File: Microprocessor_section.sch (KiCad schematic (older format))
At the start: 14 parts

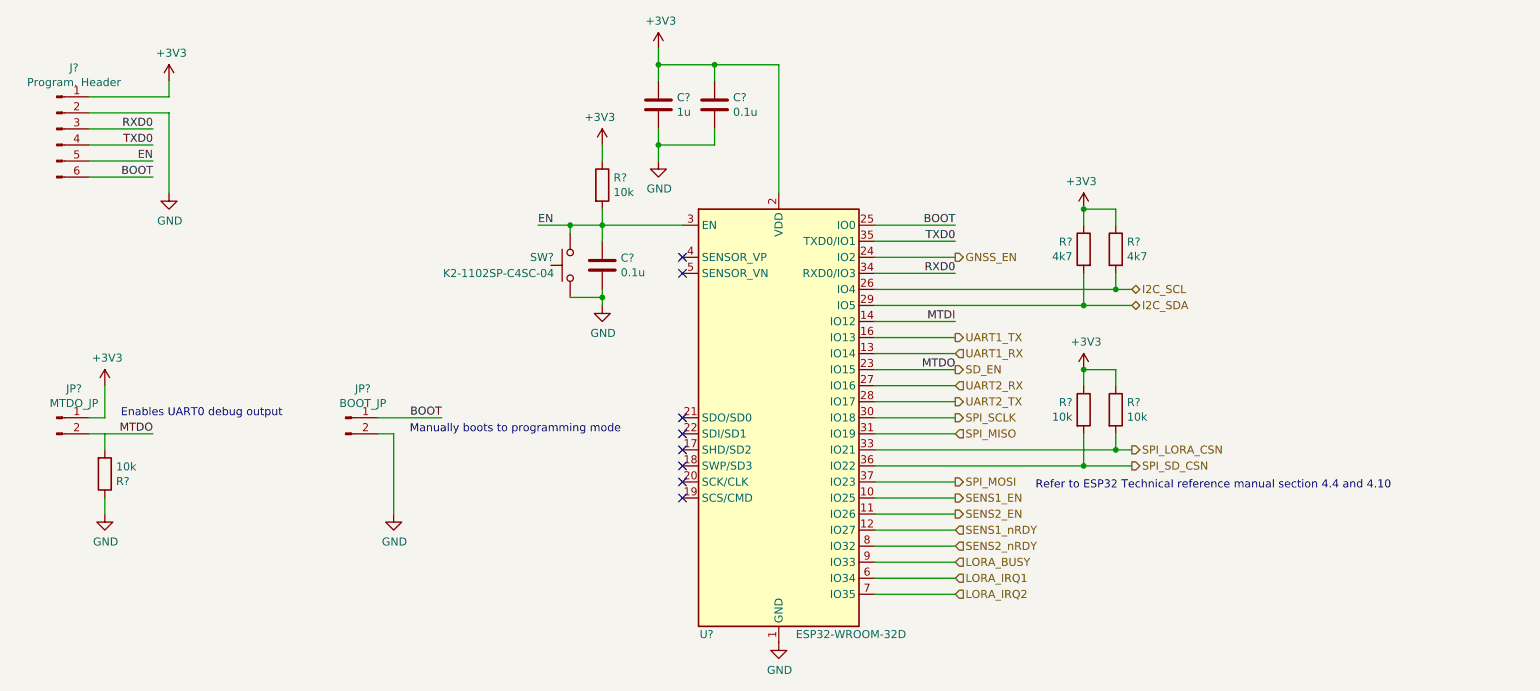
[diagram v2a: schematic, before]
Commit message: Change BME280 out for connector
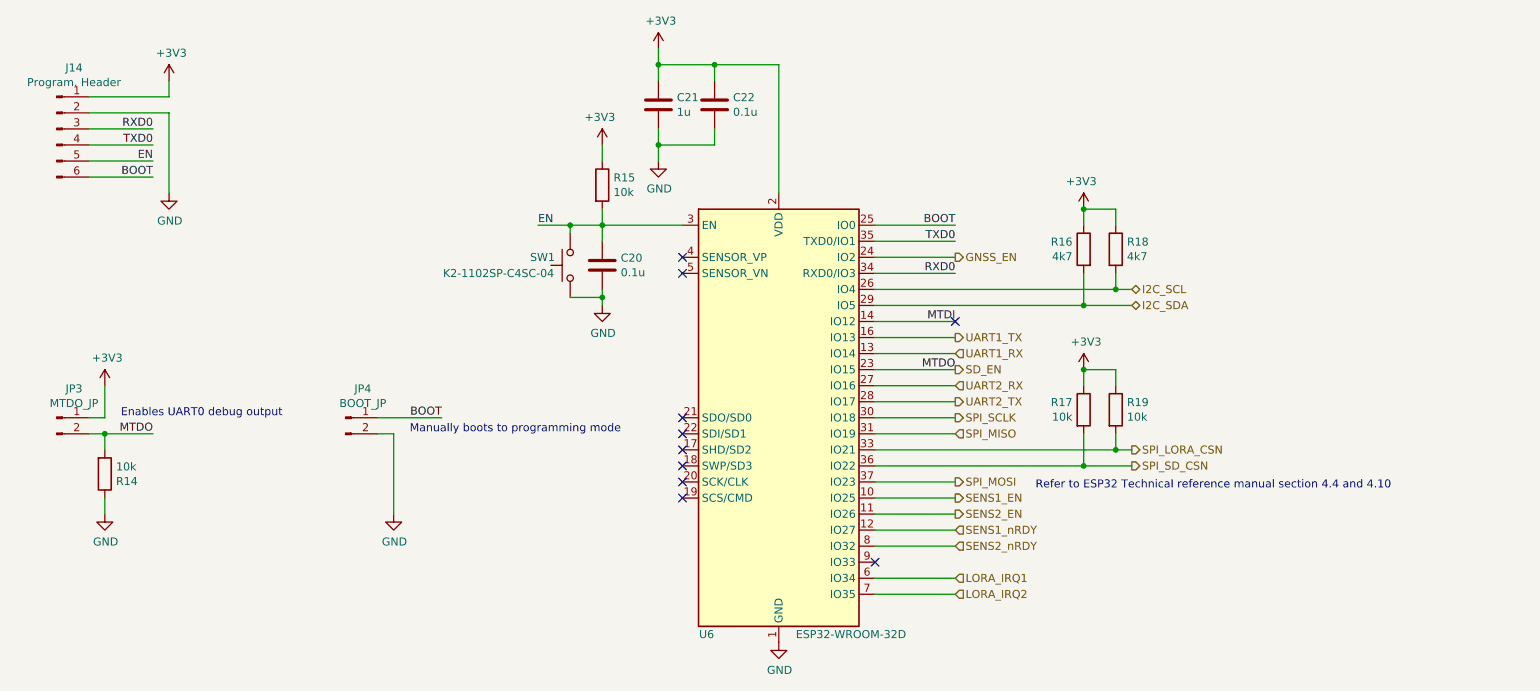
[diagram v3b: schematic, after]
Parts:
- gave numbers to parts that had none: 14
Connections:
- net SD_EN: now also R14.2
- net LORA_BUSY: no longer names the net of U6.9 (IO33)
- no-connect marks 8 -> 10
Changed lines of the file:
@@
 $EndDescr
 $Comp
-L power:GND #PWR?
+L power:GND #PWR060
 U 1 1 60B1C531
 P 2700 2600
-F 0 "#PWR?" H 2700 2350 50  0001 C CNN
+F 0 "#PWR060" H 2700 2350 50  0001 C CNN
 F 1 "GND" H 2705 2427 50  0000 C CNN
 F 2 "" H 2700 2600 50  0001 C CNN
@@
 TXD0
 $Comp
-L Connector:Conn_01x06_Male J?
+L Connector:Conn_01x06_Male J14
 U 1 1 60B18C71
 P 2000 2200
-F 0 "J?" H 2108 2581 50  0000 C CNN
+F 0 "J14" H 2108 2581 50  0000 C CNN
 F 1 "Program. Header" H 2108 2490 50  0000 C CNN
 F 2 "" H 2000 2200 50  0001 C CNN
@@
 	2700 2000 2700 1900
 $Comp
-L power:+3V3 #PWR?
+L power:+3V3 #PWR059
 U 1 1 60A521B8
 P 2700 1900
-F 0 "#PWR?" H 2700 1750 50  0001 C CNN
+F 0 "#PWR059" H 2700 1750 50  0001 C CNN
 F 1 "+3V3" H 2715 2073 50  0000 C CNN
 F 2 "" H 2700 1900 50  0001 C CNN
@@
 	5400 3200 5400 3250
 $Comp
-L power:GND #PWR?
+L power:GND #PWR063
 U 1 1 60A62E95
 P 5400 3300
-F 0 "#PWR?" H 5400 3050 50  0001 C CNN
+F 0 "#PWR063" H 5400 3050 50  0001 C CNN
 F 1 "GND" H 5405 3127 50  0000 C CNN
 F 2 "" H 5400 3300 50  0001 C CNN
@@
 $EndComp
 $Comp
-L Device:C C?
+L Device:C C20
 U 1 1 60A615B3
 P 5400 3050
-F 0 "C?" H 5515 3096 50  0000 L CNN
+F 0 "C20" H 5515 3096 50  0000 L CNN
 F 1 "0.1u" H 5515 3005 50  0000 L CNN
 F 2 "" H 5438 2900 50  0001 C CNN
@@
 	5400 2800 5400 2700
 $Comp
-L Device:R R?
+L Device:R R15
 U 1 1 60A591EA
 P 5400 2550
-F 0 "R?" H 5470 2596 50  0000 L CNN
+F 0 "R15" H 5470 2596 50  0000 L CNN
 F 1 "10k" H 5470 2505 50  0000 L CNN
 F 2 "" V 5330 2550 50  0001 C CNN
@@
 	7100 2900 7600 2900
 $Comp
-L RF_Module:ESP32-WROOM-32D U?
+L RF_Module:ESP32-WROOM-32D U6
 U 1 1 60AF9B80
 P 6500 4000
-F 0 "U?" H 6050 2650 50  0000 C CNN
+F 0 "U6" H 6050 2650 50  0000 C CNN
 F 1 "ESP32-WROOM-32D" H 6950 2650 50  0000 C CNN
 F 2 "RF_Module:ESP32-WROOM-32" H 6500 2500 50  0001 C CNN
@@
 	8600 3700 8600 3800
 $Comp
-L power:GND #PWR?
+L power:GND #PWR066
 U 1 1 60AD4CF4
 P 6500 5400
-F 0 "#PWR?" H 6500 5150 50  0001 C CNN
+F 0 "#PWR066" H 6500 5150 50  0001 C CNN
 F 1 "GND" H 6505 5227 50  0000 C CNN
 F 2 "" H 6500 5400 50  0001 C CNN
@@
 Wire Wire Line
 	7100 5000 7600 5000
-Wire Wire Line
-	7100 4900 7600 4900
 Wire Wire Line
 	7100 4100 7600 4100
@@
 Text HLabel 7600 5000 2    50   Input ~ 0
 LORA_IRQ1
-Text HLabel 7600 4900 2    50   Input ~ 0
-LORA_BUSY
 Text HLabel 7600 3000 2    50   Output ~ 0
 GNSS_EN
@@
 	5750 2300 5750 2400
 $Comp
-L power:GND #PWR?
+L power:GND #PWR065
 U 1 1 60A601F1
 P 5750 2400
-F 0 "#PWR?" H 5750 2150 50  0001 C CNN
+F 0 "#PWR065" H 5750 2150 50  0001 C CNN
 F 1 "GND" H 5755 2227 50  0000 C CNN
 F 2 "" H 5750 2400 50  0001 C CNN
@@
 	8400 3800 8400 3700
 $Comp
-L power:+3V3 #PWR?
+L power:+3V3 #PWR068
 U 1 1 60A5A46E
 P 8400 3700
-F 0 "#PWR?" H 8400 3550 50  0001 C CNN
+F 0 "#PWR068" H 8400 3550 50  0001 C CNN
 F 1 "+3V3" H 8415 3873 50  0000 C CNN
 F 2 "" H 8400 3700 50  0001 C CNN
@@
 $EndComp
 $Comp
-L Device:R R?
+L Device:R R19
 U 1 1 60A5A468
 P 8600 3950
-F 0 "R?" H 8670 3996 50  0000 L CNN
+F 0 "R19" H 8670 3996 50  0000 L CNN
 F 1 "10k" H 8670 3905 50  0000 L CNN
 F 2 "" V 8530 3950 50  0001 C CNN
@@
 $EndComp
 $Comp
-L Device:R R?
+L Device:R R17
 U 1 1 60A5A462
 P 8400 3950
-F 0 "R?" H 8330 3996 50  0000 R CNN
+F 0 "R17" H 8330 3996 50  0000 R CNN
 F 1 "10k" H 8330 3905 50  0000 R CNN
 F 2 "" V 8330 3950 50  0001 C CNN
@@
 	8600 3200 8600 3100
 $Comp
-L power:+3V3 #PWR?
+L power:+3V3 #PWR067
 U 1 1 60A5400B
 P 8400 2700
-F 0 "#PWR?" H 8400 2550 50  0001 C CNN
+F 0 "#PWR067" H 8400 2550 50  0001 C CNN
 F 1 "+3V3" H 8415 2873 50  0000 C CNN
 F 2 "" H 8400 2700 50  0001 C CNN
@@
 $EndComp
 $Comp
-L Device:R R?
+L Device:R R16
 U 1 1 60A50D69
 P 8400 2950
-F 0 "R?" H 8470 2996 50  0000 L CNN
+F 0 "R16" H 8470 2996 50  0000 L CNN
 F 1 "4k7" H 8470 2905 50  0000 L CNN
 F 2 "" V 8330 2950 50  0001 C CNN
@@
 $EndComp
 $Comp
-L Device:R R?
+L Device:R R18
 U 1 1 60A501AF
 P 8600 2950
-F 0 "R?" H 8670 2996 50  0000 L CNN
+F 0 "R18" H 8670 2996 50  0000 L CNN
 F 1 "4k7" H 8670 2905 50  0000 L CNN
 F 2 "" V 8530 2950 50  0001 C CNN
@@
 	5400 2400 5400 2300
 $Comp
-L power:+3V3 #PWR?
+L power:+3V3 #PWR062
 U 1 1 60A4456D
 P 5400 2300
-F 0 "#PWR?" H 5400 2150 50  0001 C CNN
+F 0 "#PWR062" H 5400 2150 50  0001 C CNN
 F 1 "+3V3" H 5415 2473 50  0000 C CNN
 F 2 "" H 5400 2300 50  0001 C CNN
@@
 	5750 1700 5750 1800
 $Comp
-L power:+3V3 #PWR?
+L power:+3V3 #PWR064
 U 1 1 60A42585
 P 5750 1700
-F 0 "#PWR?" H 5750 1550 50  0001 C CNN
+F 0 "#PWR064" H 5750 1550 50  0001 C CNN
 F 1 "+3V3" H 5765 1873 50  0000 C CNN
 F 2 "" H 5750 1700 50  0001 C CNN
@@
 	6100 2200 6100 2300
 $Comp
-L Device:C C?
+L Device:C C22
 U 1 1 60A3C0F5
 P 6100 2050
-F 0 "C?" H 6215 2096 50  0000 L CNN
+F 0 "C22" H 6215 2096 50  0000 L CNN
 F 1 "0.1u" H 6215 2005 50  0000 L CNN
 F 2 "" H 6138 1900 50  0001 C CNN
@@
 $EndComp
 $Comp
-L Device:C C?
+L Device:C C21
 U 1 1 60A3B0AC
 P 5750 2050
-F 0 "C?" H 5865 2096 50  0000 L CNN
+F 0 "C21" H 5865 2096 50  0000 L CNN
 F 1 "1u" H 5865 2005 50  0000 L CNN
 F 2 "" H 5788 1900 50  0001 C CNN
@@
 UART1_TX
 $Comp
-L Switch:SW_MEC_5G SW?
+L Switch:SW_MEC_5G SW1
 U 1 1 60A91701
 P 5200 3050
-F 0 "SW?" V 5150 3300 50  0000 R CNN
+F 0 "SW1" V 5150 3300 50  0000 R CNN
 F 1 "K2-1102SP-C4SC-04" V 5250 3150 50  0000 L CNN
 F 2 "" H 5200 3250 50  0001 C CNN
@@
 	5000 2800 5200 2800
 $Comp
-L Connector:Conn_01x02_Male JP?
+L Connector:Conn_01x02_Male JP3
 U 1 1 60AA0F54
 P 2000 4000
-F 0 "JP?" H 2108 4181 50  0000 C CNN
+F 0 "JP3" H 2108 4181 50  0000 C CNN
 F 1 "MTDO_JP" H 2108 4090 50  0000 C CNN
 F 2 "" H 2000 4000 50  0001 C CNN
@@
 $EndComp
 Wire Wire Line
-	2200 4100 2600 4100
+	2200 4100 2300 4100
 Text Label 2600 4100 2    50   ~ 0
 MTDO
@@
 	2200 4000 2300 4000
 $Comp
-L power:+3V3 #PWR?
+L power:+3V3 #PWR057
 U 1 1 60AB9C47
 P 2300 3800
-F 0 "#PWR?" H 2300 3650 50  0001 C CNN
+F 0 "#PWR057" H 2300 3650 50  0001 C CNN
 F 1 "+3V3" H 2315 3973 50  0000 C CNN
 F 2 "" H 2300 3800 50  0001 C CNN
@@
 $EndComp
 $Comp
-L Connector:Conn_01x02_Male JP?
+L Connector:Conn_01x02_Male JP4
 U 1 1 60ABCC26
 P 3800 4000
-F 0 "JP?" H 3908 4181 50  0000 C CNN
+F 0 "JP4" H 3908 4181 50  0000 C CNN
 F 1 "BOOT_JP" H 3908 4090 50  0000 C CNN
 F 2 "" H 3800 4000 50  0001 C CNN
@@
 	4000 4100 4100 4100
 $Comp
-L power:GND #PWR?
+L power:GND #PWR061
 U 1 1 60AC5B3B
 P 4100 4600
-F 0 "#PWR?" H 4100 4350 50  0001 C CNN
+F 0 "#PWR061" H 4100 4350 50  0001 C CNN
 F 1 "GND" H 4105 4427 50  0000 C CNN
 F 2 "" H 4100 4600 50  0001 C CNN
@@
 	2300 3800 2300 4000
 $Comp
-L Device:R R?
+L Device:R R14
 U 1 1 60AD1473
 P 2300 4350
-F 0 "R?" H 2370 4396 50  0000 L CNN
+F 0 "R14" H 2370 4396 50  0000 L CNN
 F 1 "10k" H 2370 4305 50  0000 L CNN
 F 2 "" V 2230 4350 50  0001 C CNN
@@
 $EndComp
 Wire Wire Line
-	2300 4100 2300 4200
-Wire Wire Line
 	2300 4500 2300 4600
 $Comp
-L power:GND #PWR?
+L power:GND #PWR058
 U 1 1 60AD147B
 P 2300 4600
-F 0 "#PWR?" H 2300 4350 50  0001 C CNN
+F 0 "#PWR058" H 2300 4350 50  0001 C CNN
 F 1 "GND" H 2305 4427 50  0000 C CNN
 F 2 "" H 2300 4600 50  0001 C CNN
@@
 Text Notes 8100 4450 0    50   ~ 0
 Refer to ESP32 Technical reference manual section 4.4 and 4.10\n
+NoConn ~ 7600 3400
+NoConn ~ 7100 4900
+Wire Wire Line
+	2300 4100 2300 4200
+Connection ~ 2300 4100
+Wire Wire Line
+	2300 4100 2600 4100
 $EndSCHEMATC

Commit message: Begin assigning footprints
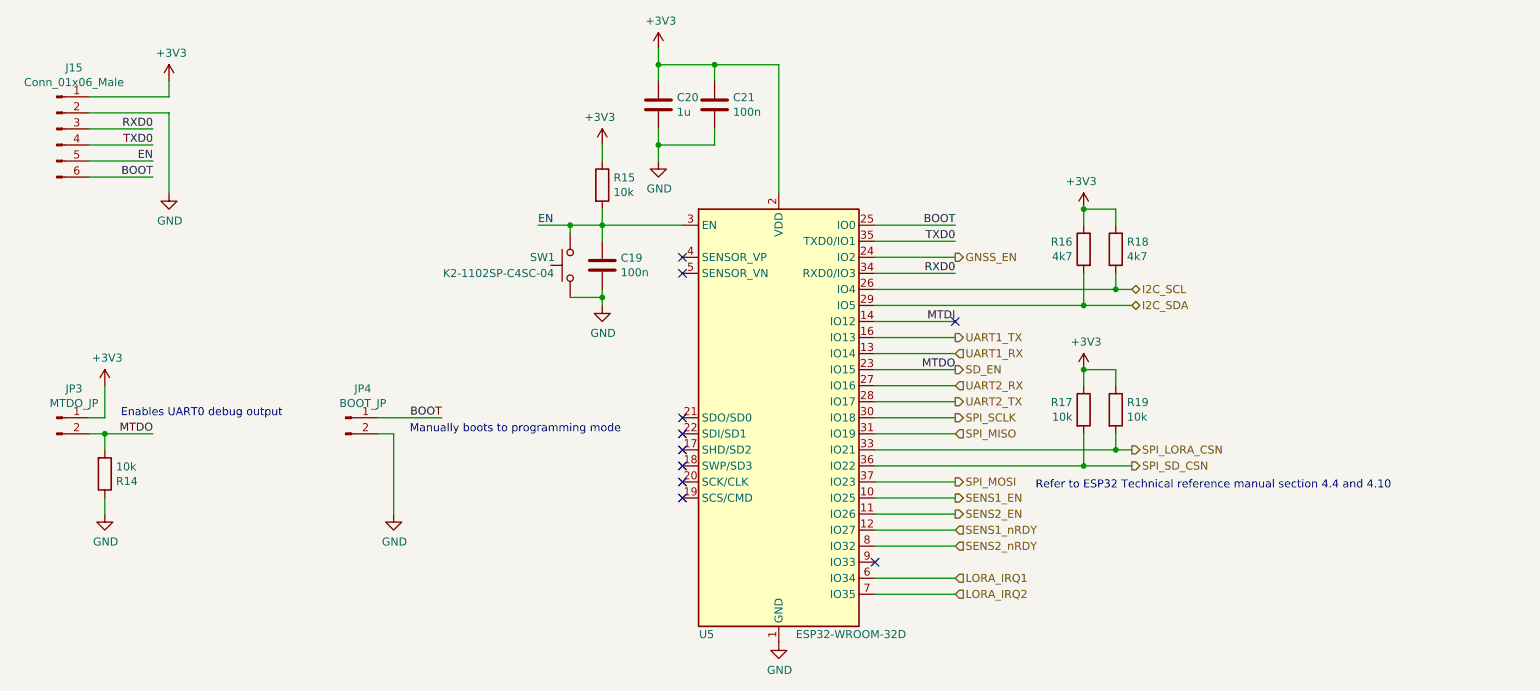
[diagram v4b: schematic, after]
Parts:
- C19: renamed from C20; value 0.1u -> 100n; footprint (none) -> Capacitor_SMD:C_0603_1608Metric; LCSC (none) -> C14663
- C20: renamed from C21; footprint (none) -> Capacitor_SMD:C_0603_1608Metric; LCSC (none) -> C15849
- C21: renamed from C22; value 0.1u -> 100n; footprint (none) -> Capacitor_SMD:C_0603_1608Metric; LCSC (none) -> C14663
- J15: renamed from J14; value Program. Header -> Conn_01x06_Male; footprint (none) -> Connector_PinHeader_2.54mm:PinHeader_1x06_P2.54mm_Vertical
- JP3, JP4: footprint (none) -> Connector_PinHeader_2.54mm:PinHeader_1x02_P2.54mm_Vertical
- R14, R15, R17, R19: footprint (none) -> Resistor_SMD:R_0603_1608Metric; LCSC (none) -> C25804
- R16, R18: footprint (none) -> Resistor_SMD:R_0603_1608Metric; LCSC (none) -> C23162
- renumbered U6 to U5
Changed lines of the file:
@@
 $EndDescr
 $Comp
-L power:GND #PWR060
+L power:GND #PWR058
 U 1 1 60B1C531
 P 2700 2600
-F 0 "#PWR060" H 2700 2350 50  0001 C CNN
+F 0 "#PWR058" H 2700 2350 50  0001 C CNN
 F 1 "GND" H 2705 2427 50  0000 C CNN
 F 2 "" H 2700 2600 50  0001 C CNN
@@
 TXD0
 $Comp
-L Connector:Conn_01x06_Male J14
+L Connector:Conn_01x06_Male J15
 U 1 1 60B18C71
 P 2000 2200
-F 0 "J14" H 2108 2581 50  0000 C CNN
-F 1 "Program. Header" H 2108 2490 50  0000 C CNN
-F 2 "" H 2000 2200 50  0001 C CNN
+F 0 "J15" H 2108 2581 50  0000 C CNN
+F 1 "Conn_01x06_Male" H 2108 2490 50  0000 C CNN
+F 2 "Connector_PinHeader_2.54mm:PinHeader_1x06_P2.54mm_Vertical" H 2000 2200 50  0001 C CNN
 F 3 "~" H 2000 2200 50  0001 C CNN
 	1    2000 2200
@@
 	2700 2000 2700 1900
 $Comp
-L power:+3V3 #PWR059
+L power:+3V3 #PWR057
 U 1 1 60A521B8
 P 2700 1900
-F 0 "#PWR059" H 2700 1750 50  0001 C CNN
+F 0 "#PWR057" H 2700 1750 50  0001 C CNN
 F 1 "+3V3" H 2715 2073 50  0000 C CNN
 F 2 "" H 2700 1900 50  0001 C CNN
@@
 	5400 3200 5400 3250
 $Comp
-L power:GND #PWR063
+L power:GND #PWR061
 U 1 1 60A62E95
 P 5400 3300
-F 0 "#PWR063" H 5400 3050 50  0001 C CNN
+F 0 "#PWR061" H 5400 3050 50  0001 C CNN
 F 1 "GND" H 5405 3127 50  0000 C CNN
 F 2 "" H 5400 3300 50  0001 C CNN
@@
 $EndComp
 $Comp
-L Device:C C20
+L Device:C C19
 U 1 1 60A615B3
 P 5400 3050
-F 0 "C20" H 5515 3096 50  0000 L CNN
-F 1 "0.1u" H 5515 3005 50  0000 L CNN
-F 2 "" H 5438 2900 50  0001 C CNN
+F 0 "C19" H 5515 3096 50  0000 L CNN
+F 1 "100n" H 5515 3005 50  0000 L CNN
+F 2 "Capacitor_SMD:C_0603_1608Metric" H 5438 2900 50  0001 C CNN
 F 3 "~" H 5400 3050 50  0001 C CNN
+F 4 "C14663" H 5400 3050 50  0001 C CNN "LCSC"
 	1    5400 3050
 	1    0    0    -1
@@
 F 0 "R15" H 5470 2596 50  0000 L CNN
 F 1 "10k" H 5470 2505 50  0000 L CNN
-F 2 "" V 5330 2550 50  0001 C CNN
+F 2 "Resistor_SMD:R_0603_1608Metric" V 5330 2550 50  0001 C CNN
 F 3 "~" H 5400 2550 50  0001 C CNN
+F 4 "C25804" H 5400 2550 50  0001 C CNN "LCSC"
 	1    5400 2550
 	1    0    0    -1
@@
 	7100 2900 7600 2900
 $Comp
-L RF_Module:ESP32-WROOM-32D U6
+L RF_Module:ESP32-WROOM-32D U5
 U 1 1 60AF9B80
 P 6500 4000
-F 0 "U6" H 6050 2650 50  0000 C CNN
+F 0 "U5" H 6050 2650 50  0000 C CNN
 F 1 "ESP32-WROOM-32D" H 6950 2650 50  0000 C CNN
 F 2 "RF_Module:ESP32-WROOM-32" H 6500 2500 50  0001 C CNN
@@
 	8600 3700 8600 3800
 $Comp
-L power:GND #PWR066
+L power:GND #PWR064
 U 1 1 60AD4CF4
 P 6500 5400
-F 0 "#PWR066" H 6500 5150 50  0001 C CNN
+F 0 "#PWR064" H 6500 5150 50  0001 C CNN
 F 1 "GND" H 6505 5227 50  0000 C CNN
 F 2 "" H 6500 5400 50  0001 C CNN
@@
 	5750 2300 5750 2400
 $Comp
-L power:GND #PWR065
+L power:GND #PWR063
 U 1 1 60A601F1
 P 5750 2400
-F 0 "#PWR065" H 5750 2150 50  0001 C CNN
+F 0 "#PWR063" H 5750 2150 50  0001 C CNN
 F 1 "GND" H 5755 2227 50  0000 C CNN
 F 2 "" H 5750 2400 50  0001 C CNN
@@
 	8400 3800 8400 3700
 $Comp
-L power:+3V3 #PWR068
+L power:+3V3 #PWR066
 U 1 1 60A5A46E
 P 8400 3700
-F 0 "#PWR068" H 8400 3550 50  0001 C CNN
+F 0 "#PWR066" H 8400 3550 50  0001 C CNN
 F 1 "+3V3" H 8415 3873 50  0000 C CNN
 F 2 "" H 8400 3700 50  0001 C CNN
@@
 F 0 "R19" H 8670 3996 50  0000 L CNN
 F 1 "10k" H 8670 3905 50  0000 L CNN
-F 2 "" V 8530 3950 50  0001 C CNN
+F 2 "Resistor_SMD:R_0603_1608Metric" V 8530 3950 50  0001 C CNN
 F 3 "~" H 8600 3950 50  0001 C CNN
+F 4 "C25804" H 8600 3950 50  0001 C CNN "LCSC"
 	1    8600 3950
 	1    0    0    -1
@@
 F 0 "R17" H 8330 3996 50  0000 R CNN
 F 1 "10k" H 8330 3905 50  0000 R CNN
-F 2 "" V 8330 3950 50  0001 C CNN
+F 2 "Resistor_SMD:R_0603_1608Metric" V 8330 3950 50  0001 C CNN
 F 3 "~" H 8400 3950 50  0001 C CNN
+F 4 "C25804" H 8400 3950 50  0001 C CNN "LCSC"
 	1    8400 3950
 	1    0    0    -1
@@
 	8600 3200 8600 3100
 $Comp
-L power:+3V3 #PWR067
+L power:+3V3 #PWR065
 U 1 1 60A5400B
 P 8400 2700
-F 0 "#PWR067" H 8400 2550 50  0001 C CNN
+F 0 "#PWR065" H 8400 2550 50  0001 C CNN
 F 1 "+3V3" H 8415 2873 50  0000 C CNN
 F 2 "" H 8400 2700 50  0001 C CNN
@@
 F 0 "R16" H 8470 2996 50  0000 L CNN
 F 1 "4k7" H 8470 2905 50  0000 L CNN
-F 2 "" V 8330 2950 50  0001 C CNN
+F 2 "Resistor_SMD:R_0603_1608Metric" V 8330 2950 50  0001 C CNN
 F 3 "~" H 8400 2950 50  0001 C CNN
+F 4 "C23162" H 8400 2950 50  0001 C CNN "LCSC"
 	1    8400 2950
 	-1   0    0    -1
@@
 F 0 "R18" H 8670 2996 50  0000 L CNN
 F 1 "4k7" H 8670 2905 50  0000 L CNN
-F 2 "" V 8530 2950 50  0001 C CNN
+F 2 "Resistor_SMD:R_0603_1608Metric" V 8530 2950 50  0001 C CNN
 F 3 "~" H 8600 2950 50  0001 C CNN
+F 4 "C23162" H 8600 2950 50  0001 C CNN "LCSC"
 	1    8600 2950
 	1    0    0    -1
@@
 	5400 2400 5400 2300
 $Comp
-L power:+3V3 #PWR062
+L power:+3V3 #PWR060
 U 1 1 60A4456D
 P 5400 2300
-F 0 "#PWR062" H 5400 2150 50  0001 C CNN
+F 0 "#PWR060" H 5400 2150 50  0001 C CNN
 F 1 "+3V3" H 5415 2473 50  0000 C CNN
 F 2 "" H 5400 2300 50  0001 C CNN
@@
 	5750 1700 5750 1800
 $Comp
-L power:+3V3 #PWR064
+L power:+3V3 #PWR062
 U 1 1 60A42585
 P 5750 1700
-F 0 "#PWR064" H 5750 1550 50  0001 C CNN
+F 0 "#PWR062" H 5750 1550 50  0001 C CNN
 F 1 "+3V3" H 5765 1873 50  0000 C CNN
 F 2 "" H 5750 1700 50  0001 C CNN
@@
 	6100 2200 6100 2300
 $Comp
-L Device:C C22
+L Device:C C21
 U 1 1 60A3C0F5
 P 6100 2050
-F 0 "C22" H 6215 2096 50  0000 L CNN
-F 1 "0.1u" H 6215 2005 50  0000 L CNN
-F 2 "" H 6138 1900 50  0001 C CNN
+F 0 "C21" H 6215 2096 50  0000 L CNN
+F 1 "100n" H 6215 2005 50  0000 L CNN
+F 2 "Capacitor_SMD:C_0603_1608Metric" H 6138 1900 50  0001 C CNN
 F 3 "~" H 6100 2050 50  0001 C CNN
+F 4 "C14663" H 6100 2050 50  0001 C CNN "LCSC"
 	1    6100 2050
 	1    0    0    -1
 $EndComp
 $Comp
-L Device:C C21
+L Device:C C20
 U 1 1 60A3B0AC
 P 5750 2050
-F 0 "C21" H 5865 2096 50  0000 L CNN
+F 0 "C20" H 5865 2096 50  0000 L CNN
 F 1 "1u" H 5865 2005 50  0000 L CNN
-F 2 "" H 5788 1900 50  0001 C CNN
+F 2 "Capacitor_SMD:C_0603_1608Metric" H 5788 1900 50  0001 C CNN
 F 3 "~" H 5750 2050 50  0001 C CNN
+F 4 "C15849" H 5750 2050 50  0001 C CNN "LCSC"
 	1    5750 2050
 	1    0    0    -1
@@
 F 0 "JP3" H 2108 4181 50  0000 C CNN
 F 1 "MTDO_JP" H 2108 4090 50  0000 C CNN
-F 2 "" H 2000 4000 50  0001 C CNN
+F 2 "Connector_PinHeader_2.54mm:PinHeader_1x02_P2.54mm_Vertical" H 2000 4000 50  0001 C CNN
 F 3 "~" H 2000 4000 50  0001 C CNN
 	1    2000 4000
@@
 	2200 4000 2300 4000
 $Comp
-L power:+3V3 #PWR057
+L power:+3V3 #PWR055
 U 1 1 60AB9C47
 P 2300 3800
-F 0 "#PWR057" H 2300 3650 50  0001 C CNN
+F 0 "#PWR055" H 2300 3650 50  0001 C CNN
 F 1 "+3V3" H 2315 3973 50  0000 C CNN
 F 2 "" H 2300 3800 50  0001 C CNN
@@
 F 0 "JP4" H 3908 4181 50  0000 C CNN
 F 1 "BOOT_JP" H 3908 4090 50  0000 C CNN
-F 2 "" H 3800 4000 50  0001 C CNN
+F 2 "Connector_PinHeader_2.54mm:PinHeader_1x02_P2.54mm_Vertical" H 3800 4000 50  0001 C CNN
 F 3 "~" H 3800 4000 50  0001 C CNN
 	1    3800 4000
@@
 	4000 4100 4100 4100
 $Comp
-L power:GND #PWR061
+L power:GND #PWR059
 U 1 1 60AC5B3B
 P 4100 4600
-F 0 "#PWR061" H 4100 4350 50  0001 C CNN
+F 0 "#PWR059" H 4100 4350 50  0001 C CNN
 F 1 "GND" H 4105 4427 50  0000 C CNN
 F 2 "" H 4100 4600 50  0001 C CNN
@@
 F 0 "R14" H 2370 4396 50  0000 L CNN
 F 1 "10k" H 2370 4305 50  0000 L CNN
-F 2 "" V 2230 4350 50  0001 C CNN
+F 2 "Resistor_SMD:R_0603_1608Metric" V 2230 4350 50  0001 C CNN
 F 3 "~" H 2300 4350 50  0001 C CNN
+F 4 "C25804" H 2300 4350 50  0001 C CNN "LCSC"
 	1    2300 4350
 	1    0    0    1
@@
 	2300 4500 2300 4600
 $Comp
-L power:GND #PWR058
+L power:GND #PWR056
 U 1 1 60AD147B
 P 2300 4600
-F 0 "#PWR058" H 2300 4350 50  0001 C CNN
+F 0 "#PWR056" H 2300 4350 50  0001 C CNN
 F 1 "GND" H 2305 4427 50  0000 C CNN
 F 2 "" H 2300 4600 50  0001 C CNN

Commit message: Finish attaching footprints for revision 1
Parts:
- SW1: footprint (none) -> co2_sensor_node:K2-1102SP-xxxC
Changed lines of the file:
@@
 F 0 "SW1" V 5150 3300 50  0000 R CNN
 F 1 "K2-1102SP-C4SC-04" V 5250 3150 50  0000 L CNN
-F 2 "" H 5200 3250 50  0001 C CNN
+F 2 "co2_sensor_node:K2-1102SP-xxxC" H 5200 3250 50  0001 C CNN
 F 3 "https://datasheet.lcsc.com/szlcsc/1811082113_Korean-Hroparts-Elec-K2-1102SP-C4SC-04_C127509.pdf" H 5200 3250 50  0001 C CNN
 F 4 "https://lcsc.com/product-detail/Tactile-Switches_Korean-Hroparts-Elec-K2-1102SP-C4SC-04_C127509.html/?href=jlc-SMT" V 5200 3050 50  0001 C CNN "LCSC"
